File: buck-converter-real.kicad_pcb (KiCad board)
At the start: 4 copper layers, 64 x 64 mm, 56 parts, among them J1 Conn_01x02_Pin, J1 USB_C_Receptacle_USB2.0_16P, J10 I2C1, J11 JST_01x04, J2 SOL 24V, J3 Battery out (3V6-4V2) NiMH 3S, J5 UART 2, J6 DM3CS-SF, J7 UART 1, J9 SWD, Q2 CSD18540Q5B - 60-V, SW2 SW_Omron_B3FS, U1 AP2112K-3.3 (3V3 LDO), U2 CH32V203K8T6, U5 LM5109BMA (Mosfet Driver), U6 78L12L (12V LDO) (35V max), Y1 8MHz 20pF

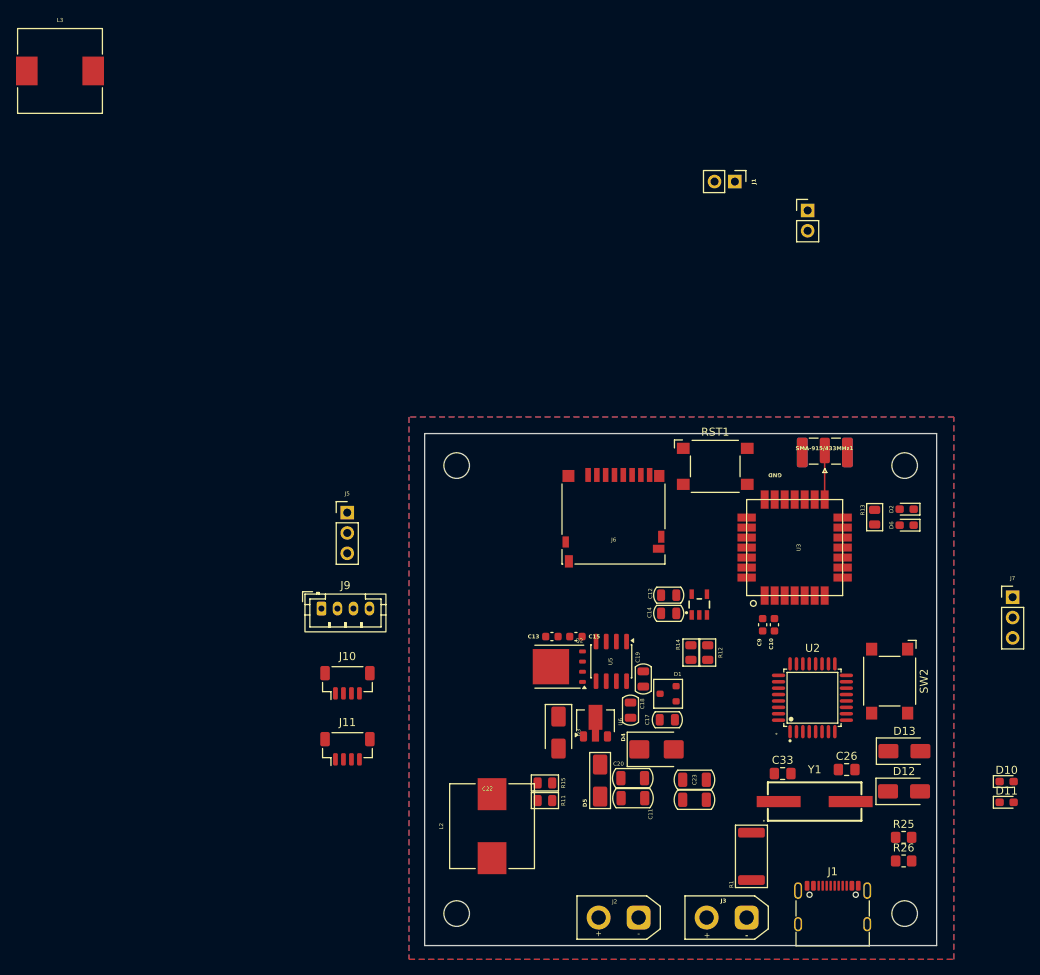
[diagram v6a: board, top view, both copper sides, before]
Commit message: Update layout/schematic - remove gpio expander, shuffle components
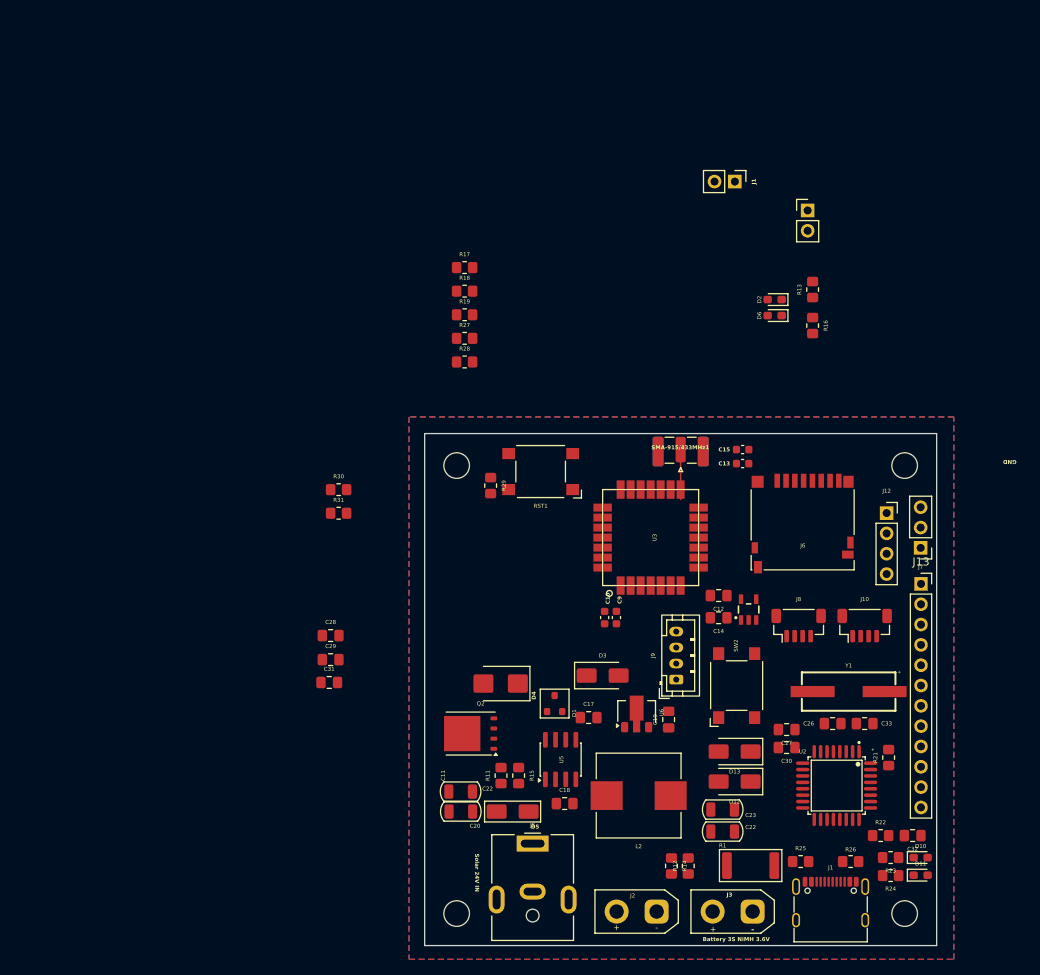
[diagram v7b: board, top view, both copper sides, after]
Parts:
- removed J11: JST_01x04, Connector_JST:JST_SH_BM04B-SRSS-TB_1x04-1MP_P1.00mm_Vertical
- removed L3: 10uH ±20% 18mΩ Molded, Inductor_SMD:L_10.4x10.4_H4.8
- added C27: 100n 50V, Capacitor_SMD:C_0805_2012Metric_Pad1.18x1.45mm_HandSolder, F.Cu at (113.2, 105.0)
- added C28: 100nF 50V, Capacitor_SMD:C_0805_2012Metric_Pad1.18x1.45mm_HandSolder, F.Cu at (56.2, 93.2)
- added C29: 100nF 50V, Capacitor_SMD:C_0805_2012Metric_Pad1.18x1.45mm_HandSolder, F.Cu at (56.2, 96.3)
- added C30: 1uF 25V, Capacitor_SMD:C_0805_2012Metric_Pad1.18x1.45mm_HandSolder, F.Cu at (113.2, 107.2)
- added C31: 10uF, Capacitor_SMD:C_0805_2012Metric_Pad1.18x1.45mm_HandSolder, F.Cu at (56.1, 99.1)
- added C32: 100nF 50V, Capacitor_SMD:C_0805_2012Metric_Pad1.18x1.45mm_HandSolder, F.Cu at (129.0, 118.2)
- added J12: Conn_01x04, Connector_PinSocket_2.54mm:PinSocket_1x04_P2.54mm_Vertical, F.Cu at (125.8, 77.9)
- added J13: Conn_01x12, Connector_PinSocket_2.54mm:PinSocket_1x12_P2.54mm_Vertical, F.Cu at (130.0, 86.8)
- added J8: I2C1, Connector_JST:JST_SH_BM04B-SRSS-TB_1x04-1MP_P1.00mm_Vertical, F.Cu at (114.8, 92.0)
- added R16: 10K, Resistor_SMD:R_0805_2012Metric_Pad1.20x1.40mm_HandSolder, F.Cu at (116.5, 54.5)
- added R17: 10K, Resistor_SMD:R_0805_2012Metric_Pad1.20x1.40mm_HandSolder, F.Cu at (73.0, 47.2)
- added R18: 10K, Resistor_SMD:R_0805_2012Metric_Pad1.20x1.40mm_HandSolder, F.Cu at (73.0, 50.2)
- added R19: 10K, Resistor_SMD:R_0805_2012Metric_Pad1.20x1.40mm_HandSolder, F.Cu at (73.0, 53.1)
- added R21: 10K, Resistor_SMD:R_0805_2012Metric_Pad1.20x1.40mm_HandSolder, F.Cu at (126.0, 108.5)
- added R22: 10K, Resistor_SMD:R_0805_2012Metric_Pad1.20x1.40mm_HandSolder, F.Cu at (125.0, 118.2)
- added R23: 10K, Resistor_SMD:R_0805_2012Metric_Pad1.20x1.40mm_HandSolder, F.Cu at (126.2, 121.0)
- added R24: 10K, Resistor_SMD:R_0805_2012Metric_Pad1.20x1.40mm_HandSolder, F.Cu at (126.2, 123.2)
- added R27: 4.7K, Resistor_SMD:R_0805_2012Metric_Pad1.20x1.40mm_HandSolder, F.Cu at (73.0, 56.1)
- added R28: 4.7K, Resistor_SMD:R_0805_2012Metric_Pad1.20x1.40mm_HandSolder, F.Cu at (73.0, 59.0)
- added R29: 10K, Resistor_SMD:R_0805_2012Metric_Pad1.20x1.40mm_HandSolder, F.Cu at (76.2, 74.5)
- added R30: 4.7K, Resistor_SMD:R_0805_2012Metric_Pad1.20x1.40mm_HandSolder, F.Cu at (57.2, 75.0)
- added R31: 4.7K, Resistor_SMD:R_0805_2012Metric_Pad1.20x1.40mm_HandSolder, F.Cu at (57.2, 78.0)
- C12, C14, C17, C18, C19: footprint PCM_Capacitor_SMD_AKL:C_0805_2012Metric -> Capacitor_SMD:C_0805_2012Metric_Pad1.18x1.45mm_HandSolder
- J5: value UART 2 -> Barrel_Jack_MountingPin; footprint Connector_PinHeader_2.54mm:PinHeader_1x03_P2.54mm_Vertical -> Connector_BarrelJack:BarrelJack_CUI_PJ-063AH_Horizontal
- R11, R12, R13, R14, R15: footprint PCM_Resistor_SMD_AKL:R_0805_2012Metric -> Resistor_SMD:R_0805_2012Metric_Pad1.20x1.40mm_HandSolder
- moved J10 65.0 mm to (123.0, 92.0)
- moved J5 47.4 mm to (81.5, 119.2)
- moved J9 45.2 mm to (99.5, 98.8), turned to 90 degrees
- moved C13 32.2 mm to (107.8, 71.8)
- moved C15 31.3 mm to (107.8, 70.0), turned to 180 degrees
- moved D2 31.0 mm to (111.8, 51.2)
- moved D6 31.0 mm to (111.8, 53.2)
- moved R13 29.5 mm to (116.5, 50.0), turned to 90 degrees
- moved R14 26.8 mm to (98.8, 122.0)
- moved R12 26.8 mm to (101.0, 122.0)
- moved J6 23.7 mm to (115.2, 79.2)
- moved C20 21.9 mm to (72.5, 115.2), turned to 180 degrees
- moved RST1 21.8 mm to (82.5, 72.8), turned to 180 degrees
- moved C11 21.5 mm to (72.5, 112.8), turned to 180 degrees
- moved C10 21.2 mm to (90.5, 91.0), turned to -90 degrees
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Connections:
- net Net-(D1-A2) renamed /12V-OUT-LDO
- net Net-(D4-K) renamed /Solar In
- J10 pad 1: /I2C-1-SCL -> /I2C-2-SCL
- J10 pad 2: /I2C-1-SDA -> /I2C-2-SCA
- J10 pad MP: (no net) -> GND
- J5 pad 1: GND -> /Solar +
- J5 pad 2: /UART-2-RX -> GND
- J6 pad SH: (no net) -> GND
- RST1 pad 1: /MCU-RST -> /WIO-RST
- U2 pad 10: unconnected-(U2-PA4/ADC4-Pad10) -> Net-(J13-Pin_5)
- U2 pad 11: unconnected-(U2-PA5/ADC5-Pad11) -> Net-(J13-Pin_6)
- U2 pad 12: unconnected-(U2-PA6/ADC6-Pad12) -> Net-(J13-Pin_7)
- U2 pad 13: unconnected-(U2-PA7/ADC7-Pad13) -> Net-(J13-Pin_8)
- U2 pad 14: unconnected-(U2-PB0/ADC8-Pad14) -> Net-(J13-Pin_11)
- U2 pad 15: unconnected-(U2-PB1/ADC9-Pad15) -> Net-(J13-Pin_12)
- U2 pad 18: unconnected-(U2-PA8-Pad18) -> Net-(J13-Pin_9)
- U2 pad 25: unconnected-(U2-PA15-Pad25) -> Net-(J13-Pin_10)
- U2 pad 28: unconnected-(U2-PB5-Pad28) -> /WIO-RST
- U2 pad 6: unconnected-(U2-PA0/WKUP/ADC0-Pad6) -> Net-(J13-Pin_1)
- U2 pad 7: unconnected-(U2-PA1/ADC1-Pad7) -> Net-(J13-Pin_2)
- U2 pad 8: unconnected-(U2-PA2/ADC2-Pad8) -> Net-(J13-Pin_3)
- U2 pad 9: unconnected-(U2-PA3/ADC3-Pad9) -> Net-(J13-Pin_4)
- U3 pad 17: /MCU-RST -> /WIO-RST
- U3 pad 18: /UART-2-RX -> /UART-WIO-RX
- U3 pad 19: /UART-2-TX -> /UART-WIO-TX
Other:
- board text added: "Battery 3S NiMH 3.6V"
- board text added: "COATL Forest Sensor Platform V1"
- board text added: "Solar 24V IN"
- board text removed: "COATL Forest Sensor Platform V0.3"

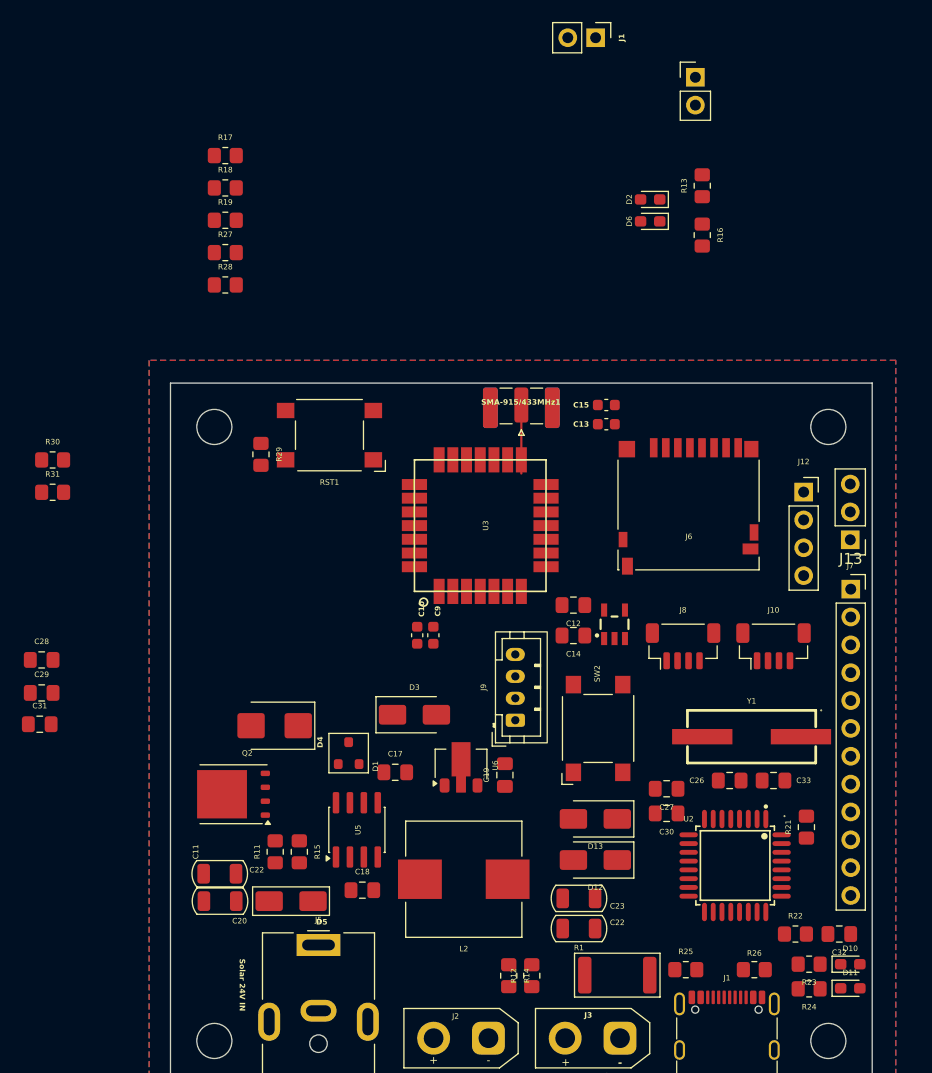
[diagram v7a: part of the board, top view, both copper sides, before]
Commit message: Update layout - Inital layout all items in area
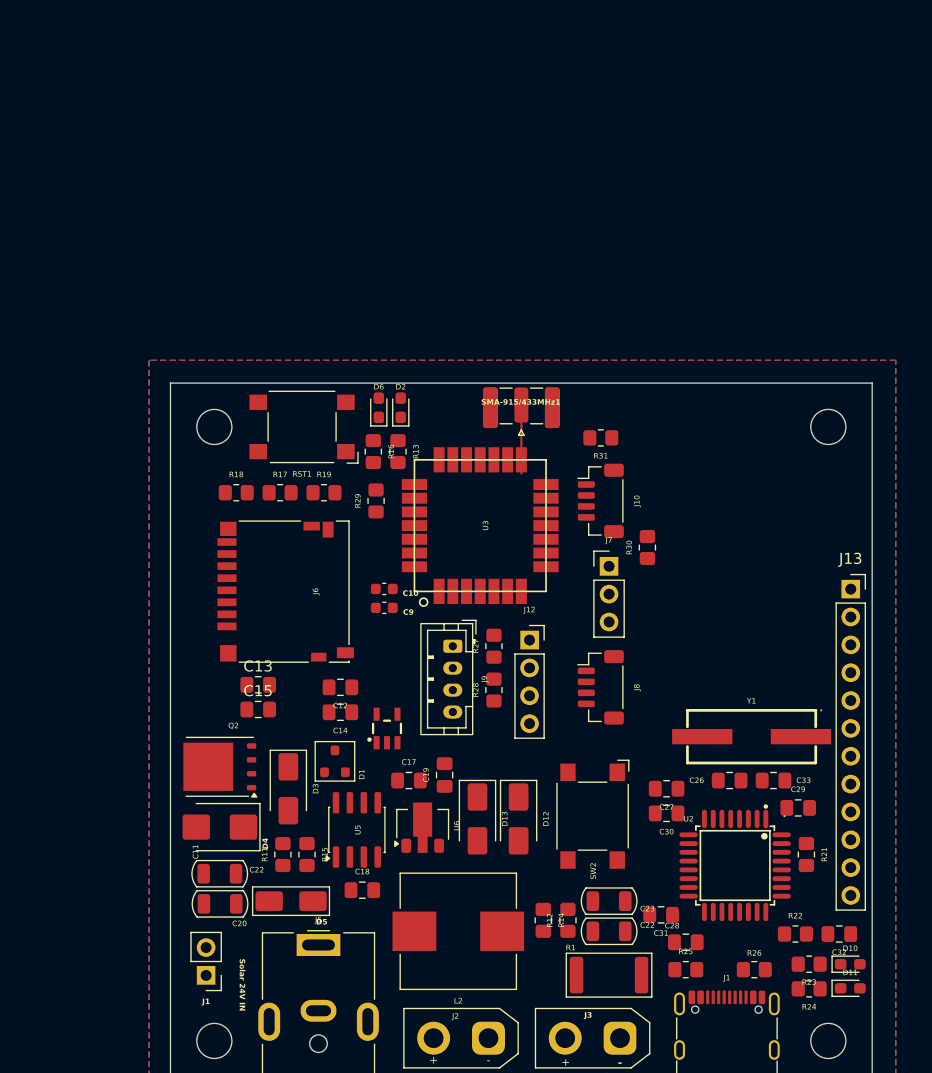
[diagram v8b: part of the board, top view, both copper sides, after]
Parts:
- removed GPIO1: GPIO, Connector_PinHeader_2.54mm:PinHeader_1x02_P2.54mm_Vertical
- C13, C15: footprint Capacitor_SMD:C_0603_1608Metric -> Capacitor_SMD:C_0805_2012Metric_Pad1.18x1.45mm_HandSolder
- moved J1 92.6 mm to (71.2, 122.0), turned to 180 degrees
- moved C29 69.8 mm to (125.2, 106.8)
- moved C28 64.1 mm to (115.0, 119.0), turned to 180 degrees
- moved C31 59.3 mm to (112.8, 116.5), turned to 180 degrees
- moved R30 54.8 mm to (111.5, 83.0), turned to 90 degrees
- moved R31 50.2 mm to (107.2, 73.0), turned to 180 degrees
- moved R28 44.3 mm to (97.5, 96.0), turned to 90 degrees
- moved R27 43.5 mm to (97.5, 92.0), turned to 90 degrees
- moved C15 42.2 mm to (76.0, 97.8), turned to 0 degrees
- moved C13 39.7 mm to (76.0, 95.5), turned to 0 degrees
- moved J6 37.6 mm to (78.5, 87.0), turned to -90 degrees
- moved R13 36.9 mm to (88.8, 74.2), turned to -90 degrees
- moved R16 35.9 mm to (86.5, 74.2)
- moved R17 31.2 mm to (78.0, 78.0)
- moved D6 30.0 mm to (87.0, 70.2), turned to 90 degrees
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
